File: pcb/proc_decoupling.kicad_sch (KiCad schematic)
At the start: 24 parts, among them U1 XC6SLX9-TQG144

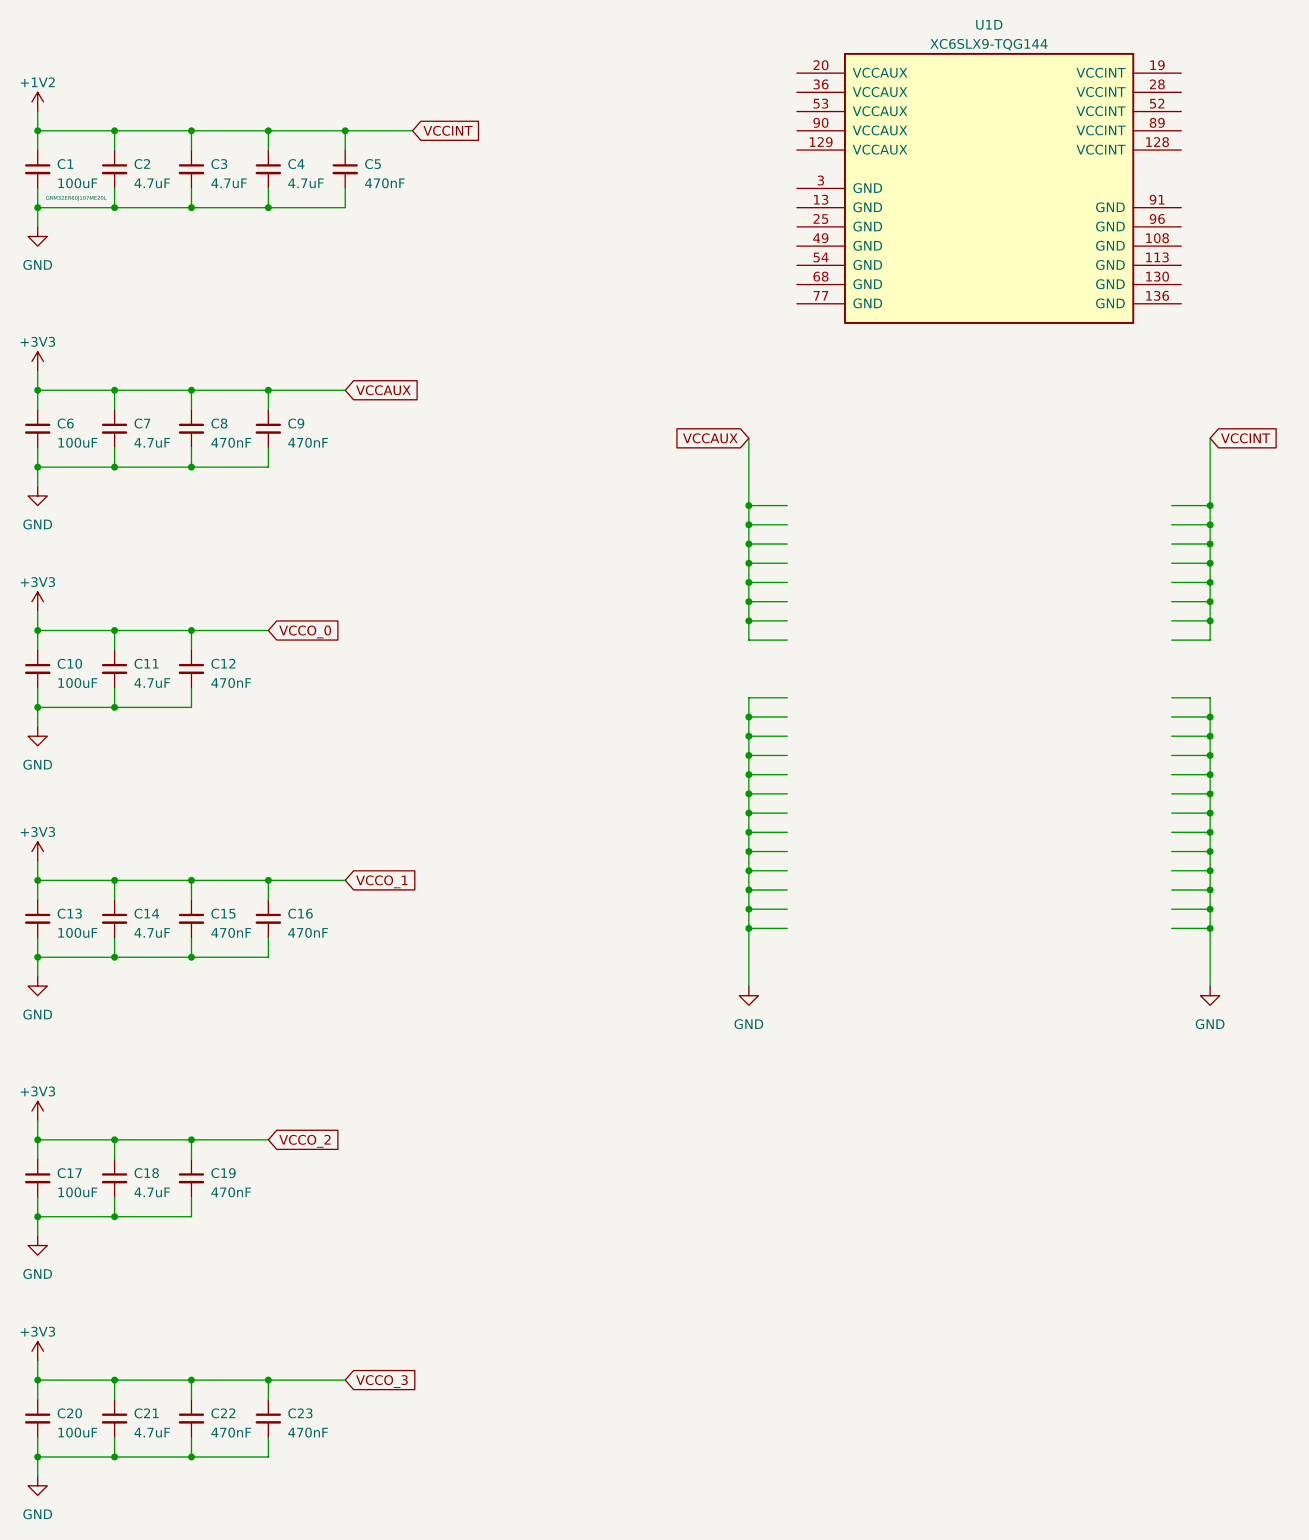
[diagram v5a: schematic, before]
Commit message: route pol
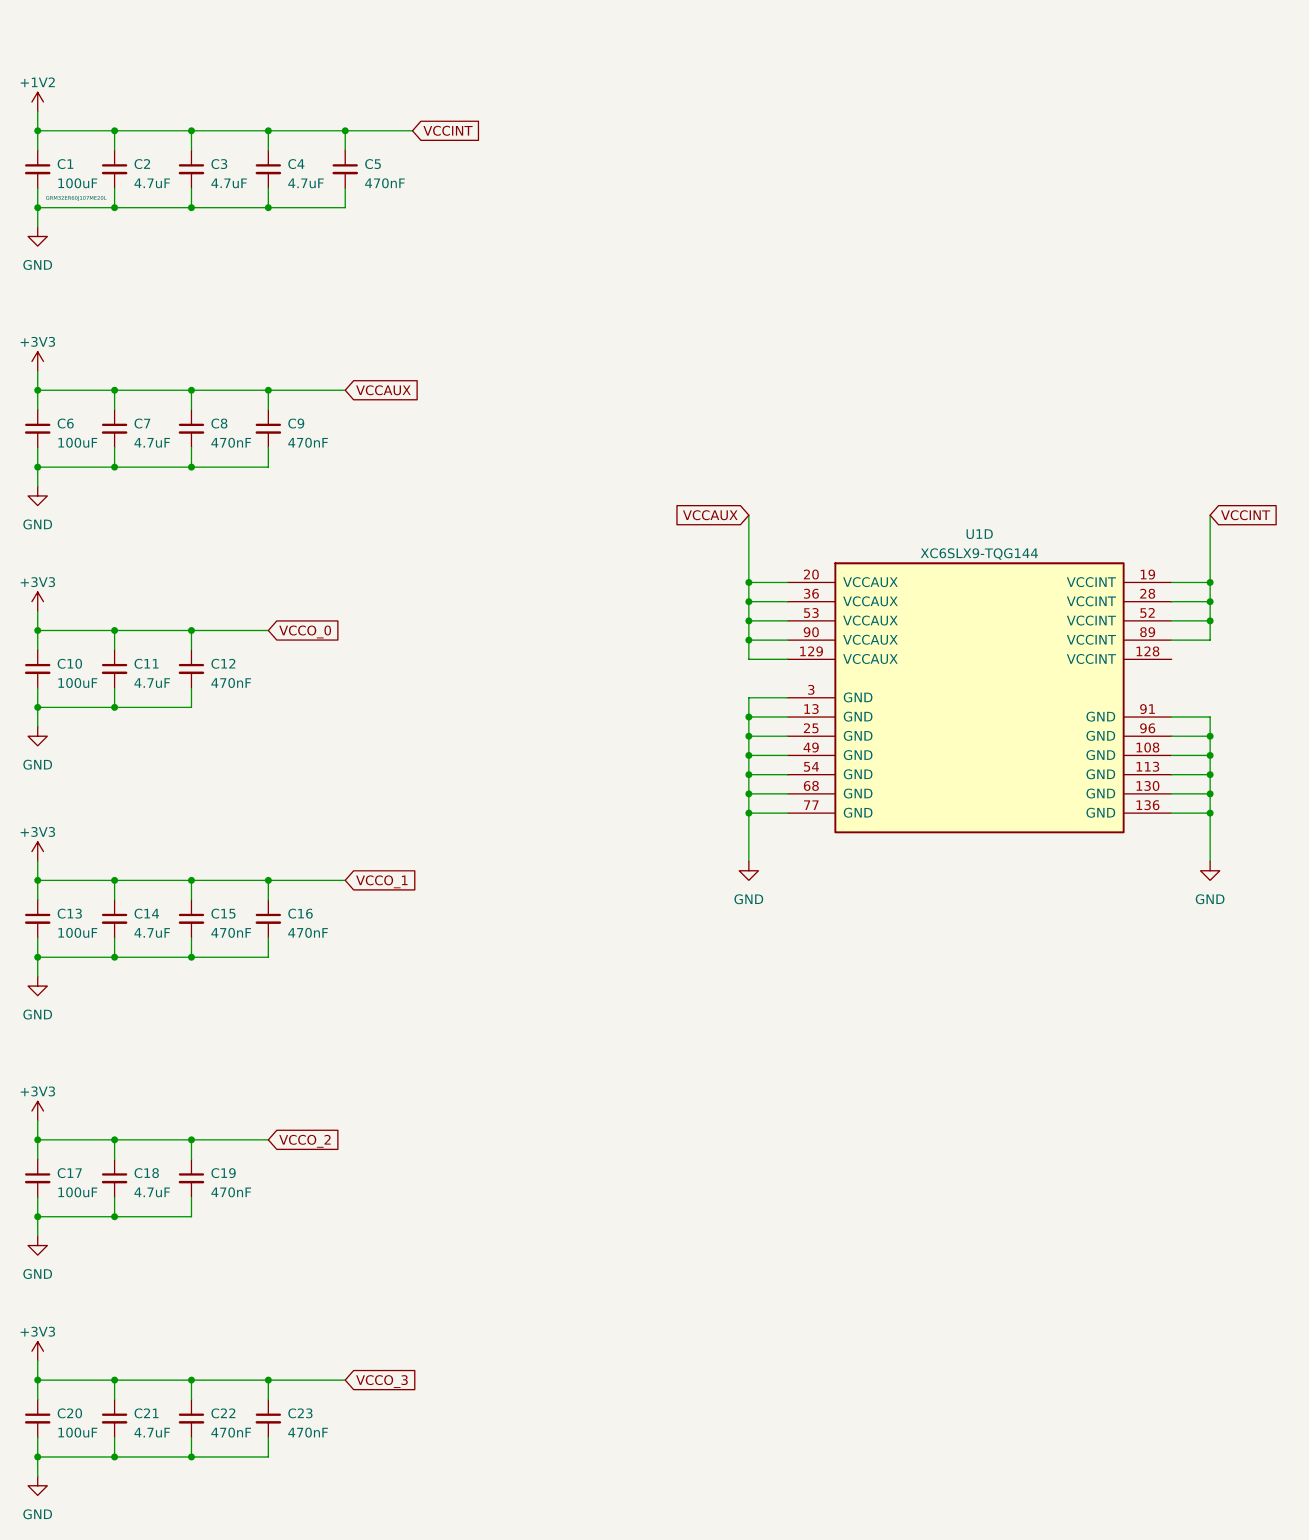
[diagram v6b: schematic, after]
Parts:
- C1: footprint Capacitor_SMD:C_1210_3225Metric -> Capacitor_SMD:C_0603_1608Metric
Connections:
- net +1V2: now also U1.19 (VCCINT), U1.28 (VCCINT), U1.52 (VCCINT), U1.89 (VCCINT)
- net +3V3: now also U1.129 (VCCAUX), U1.20 (VCCAUX), U1.36 (VCCAUX), U1.53 (VCCAUX), U1.90 (VCCAUX)
- net GND: now also U1.108 (GND), U1.113 (GND), U1.13 (GND), U1.130 (GND), U1.136 (GND), U1.25 (GND), U1.3 (GND), U1.49 (GND), U1.54 (GND), U1.68 (GND), U1.77 (GND), U1.91 (GND), U1.96 (GND)
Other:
- moved on the sheet: U1D

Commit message: add decoupling caps
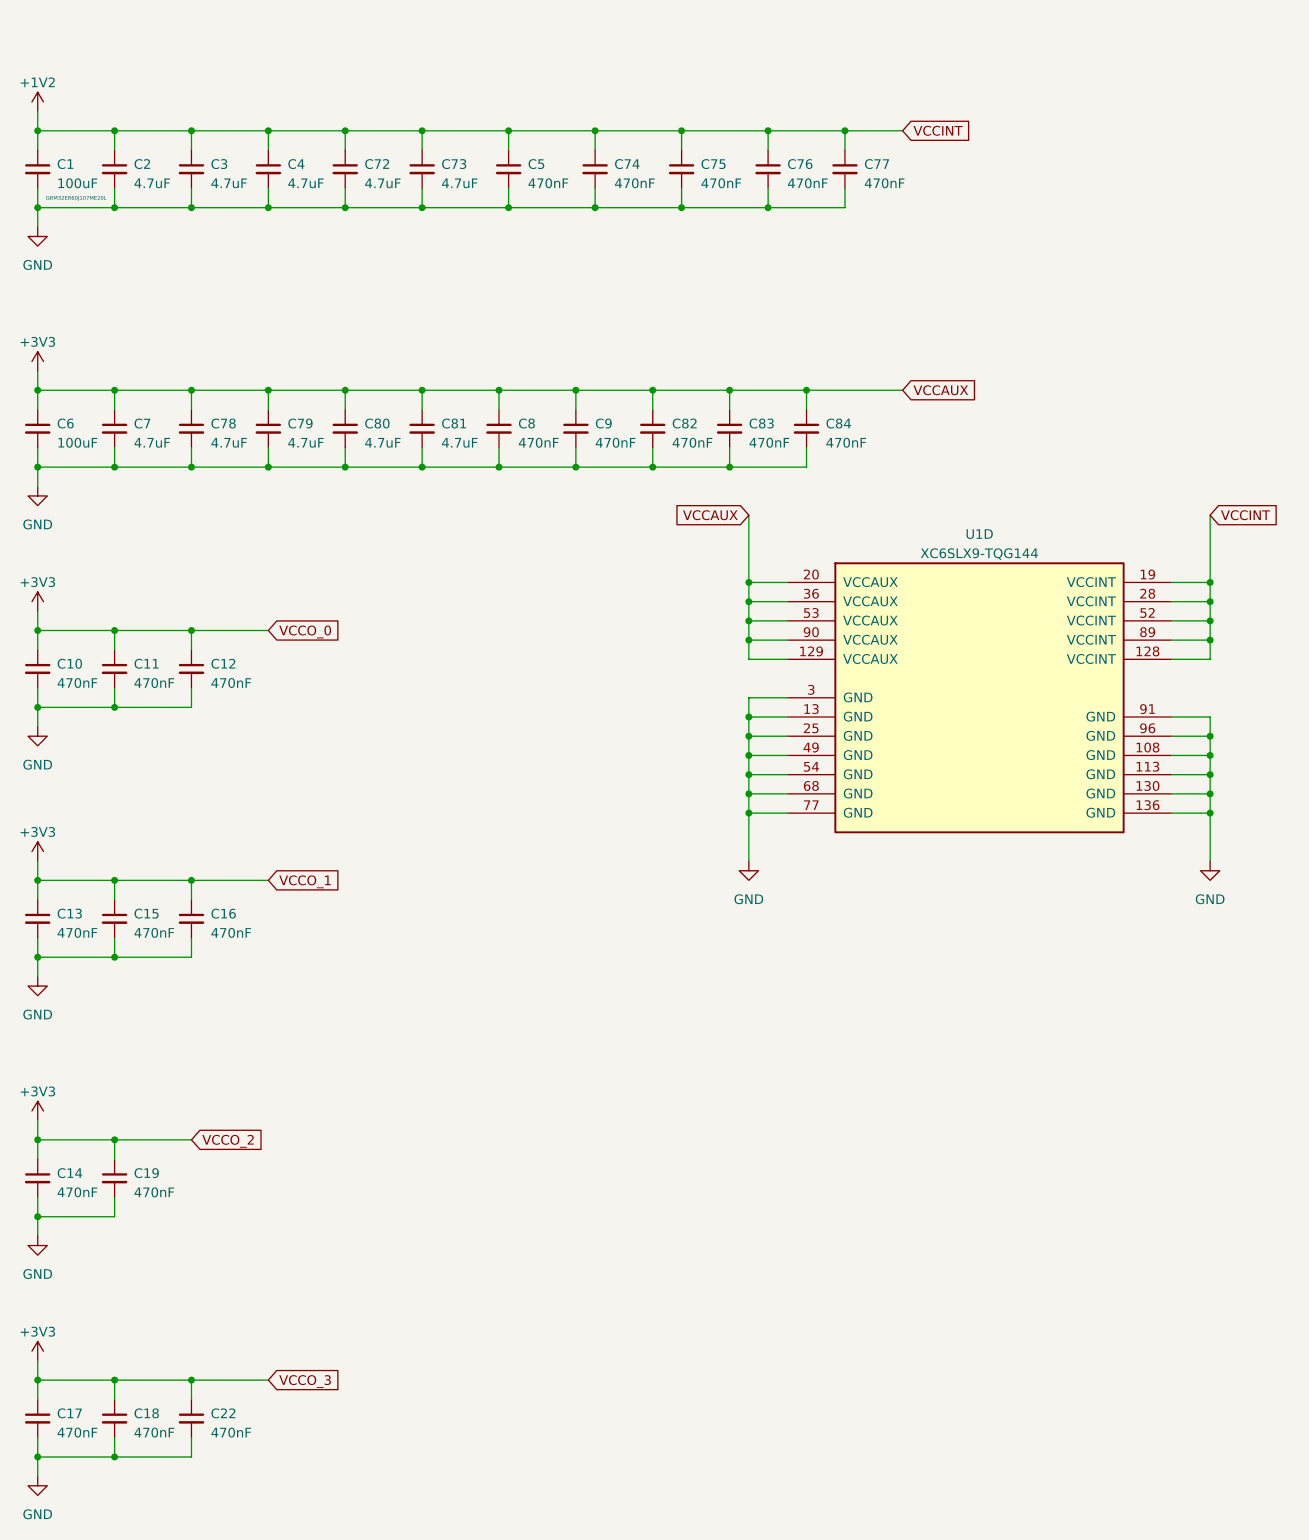
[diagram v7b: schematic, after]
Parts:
- removed C20: 100uF, Capacitor_SMD:C_1210_3225Metric, symbol Device:C_Small
- removed C21: 4.7uF, Capacitor_SMD:C_0805_2012Metric, symbol Device:C_Small
- removed C23: 470nF, Capacitor_SMD:C_0402_1005Metric, symbol Device:C_Small
- added C72, C73, C78, C79, C80, C81: 4.7uF, Capacitor_SMD:C_0805_2012Metric, symbol Device:C_Small
- added C74, C75, C76, C77, C82, C83, C84: 470nF, Capacitor_SMD:C_0402_1005Metric, symbol Device:C_Small
- C1: footprint Capacitor_SMD:C_0603_1608Metric -> Capacitor_SMD:C_1210_3225Metric
- C10, C13, C17: value 100uF -> 470nF; footprint Capacitor_SMD:C_1210_3225Metric -> Capacitor_SMD:C_0402_1005Metric
- C11, C14, C18: value 4.7uF -> 470nF; footprint Capacitor_SMD:C_0805_2012Metric -> Capacitor_SMD:C_0402_1005Metric
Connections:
- net +1V2: now also U1.128 (VCCINT), C72.1, C73.1, C74.1, C75.1, C76.1, C77.1
- net +3V3: now also C78.1, C79.1, C80.1, C81.1, C82.1, C83.1, C84.1
- net GND: now also C72.2, C73.2, C74.2, C75.2, C76.2, C77.2, C78.2, C79.2, C80.2, C81.2, C82.2, C83.2, C84.2
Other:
- moved on the sheet: C15, C16, C19, C5, C8, C9
